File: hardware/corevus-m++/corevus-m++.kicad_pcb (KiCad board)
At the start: 4 copper layers, 100 x 64 mm, 154 parts, among them J1 XH, J2 XH, J3 USB 2.0, J4 Power In, J5 Power In, J6 1x2P, SW1 RST, SW2 BOOT, T1 V_{SA}, T10 MOSI, T11 Gnd, T12 MISO, T13 3.3V, T14 Therm, T15 V_{SA}, T16 SClk, T17 MOSI, T18 Gnd, T19 MISO, T2 SClk, T20 3.3V, T21 Therm, T22 V_{SA}, T23 SClk, T24 MOSI, T25 Gnd, T26 MISO, T27 3.3V, T28 Therm, T29 CS, T3 MOSI, T30 CS, T31 CS, T32 CS, T33 CS, T34 CS, T35 CS, T36 CS, T37 En, T38 En, T39 En, T4 Gnd, T40 En, T41 En, T42 En, T43 En, T44 En, T45 Dir, T46 Dir, T47 Dir, T48 Dir, T49 Dir, T5 MISO, T50 Dir, T51 Dir, T52 Dir, T53 Gnd, T54 Gnd, T55 Gnd, T56 Gnd, T57 Gnd, T58 Gnd, T59 Gnd, T6 3.3V, T60 Gnd, T61 Step, T62 Step, T63 Step, T64 Step, T65 Step, T66 Step, T67 Step, T68 Step, T69 Diag, T7 Therm, T70 Diag, T71 Diag, T72 Diag, T73 Diag, T74 Diag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

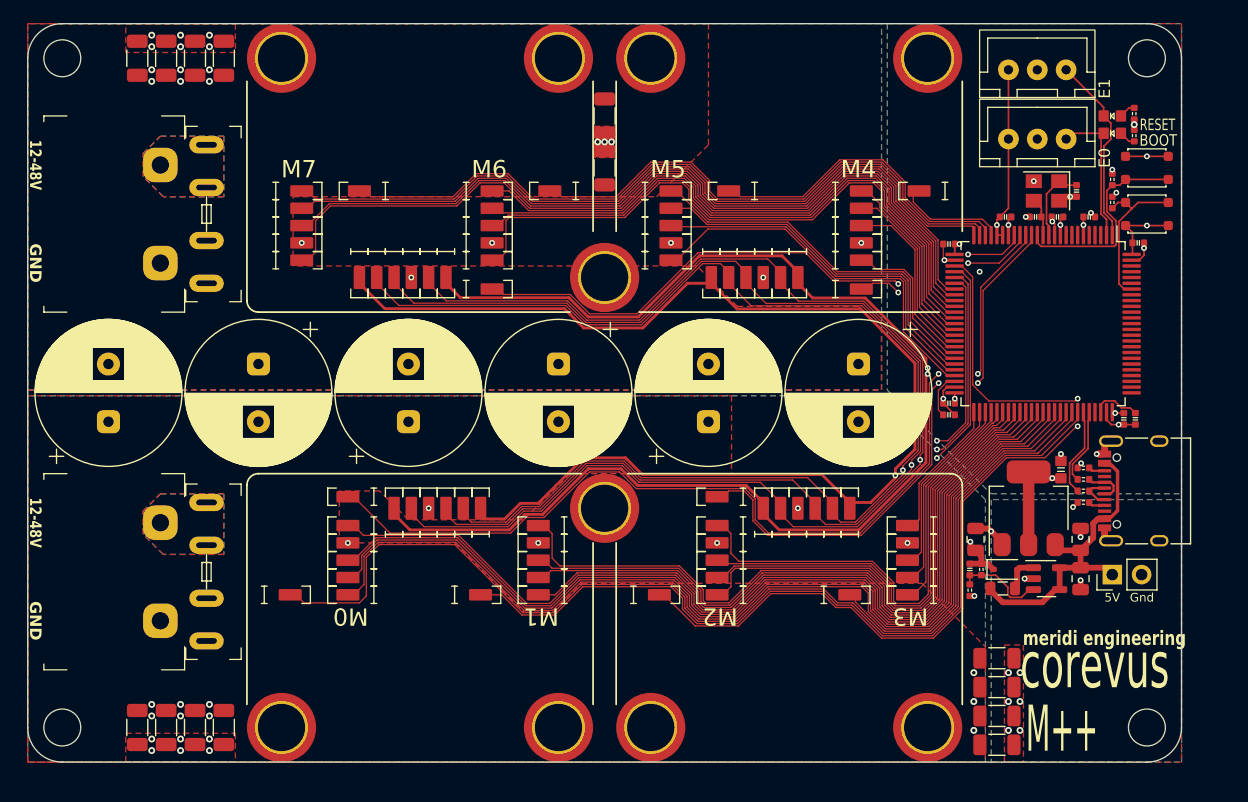
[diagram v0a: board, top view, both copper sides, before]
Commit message: corevus toolboard v0.2 release (working), corevus-g v0.2 release (very much not working), m++ v0.1 (not working, needs a lot of bodges)
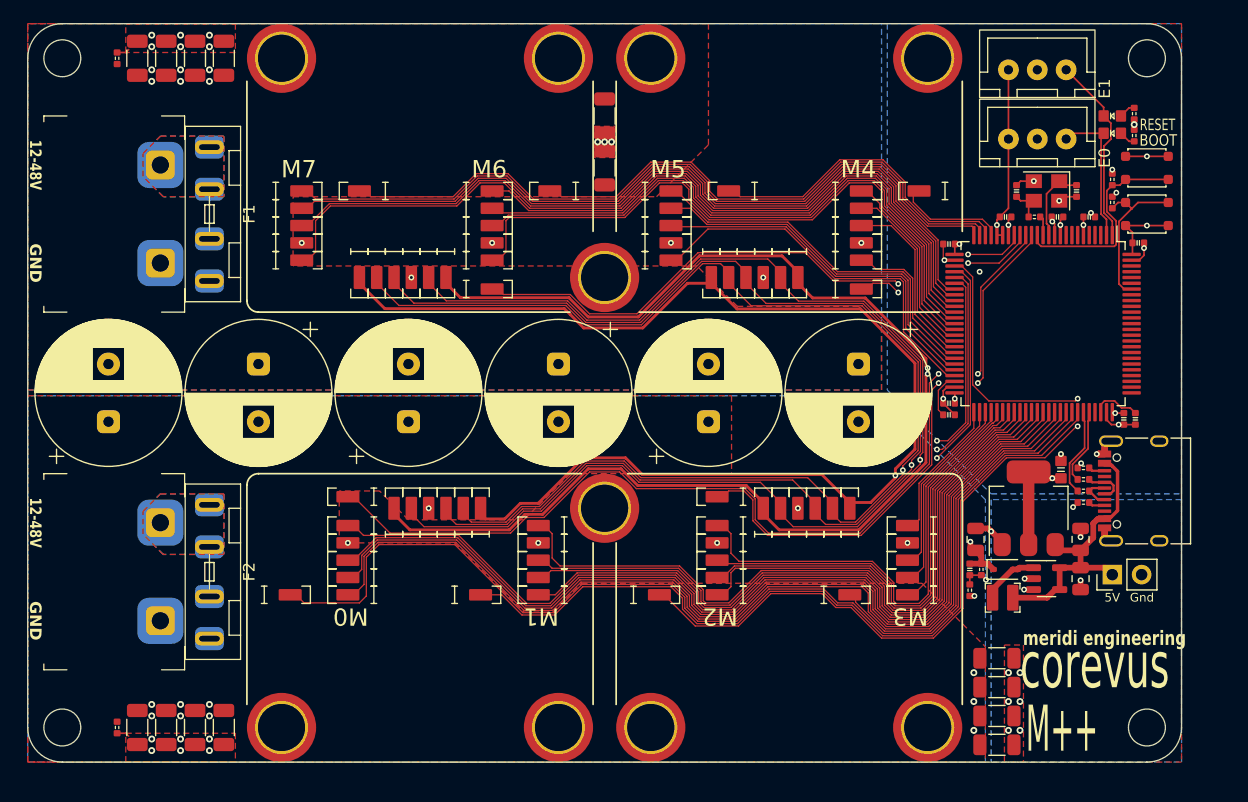
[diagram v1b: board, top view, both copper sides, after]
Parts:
- added R11: 1kΩ, AlphaLib:0402R, F.Cu at (197.2, 46.8)
- added R12: 200kΩ, AlphaLib:0402R, F.Cu at (117.8, 33.0)
- added R13: 200kΩ, AlphaLib:0402R, F.Cu at (117.8, 91.0)
- C11, C12, C13, C14, C15, C16: value 470μF 63V -> 390μF 63V
- C3, C4: value 15pF -> 16pF
- F1, F2: footprint corevus:XF-505P -> corevus:XF-506P
- L1: footprint Inductor_SMD:L_0805_2012Metric -> corevus:L_Changjiang_FTC2520
- T69, T70, T71, T72, T73, T74, T75, T76: value Diag -> Stall
- Y1: value 12 MHz -> 25 MHz
- moved C4 2.79 mm to (195.7, 44.5), turned to -90 degrees
- moved L1 0.80 mm to (194.5, 79.8)
- moved F1 0.25 mm to (125.8, 46.5)
- moved F2 0.25 mm to (125.8, 77.5)
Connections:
- net /_{M0}Diag renamed /_{M0}Stall
- net /_{M1}Diag renamed /_{M1}Stall
- net /_{M2}Diag renamed /_{M2}Stall
- net /_{M3}Diag renamed /_{M3}Stall
- net /_{M4}Diag renamed /_{M4}Stall
- net /_{M5}Diag renamed /_{M5}Stall
- net /_{M6}Diag renamed /_{M6}Stall
- net /_{M7}Diag renamed /_{M7}Stall
- C4 pad 2: Net-(U3-PH1) -> Net-(C4-Pad2)
- Y1 pad 3: Net-(U3-PH1) -> Net-(C4-Pad2)
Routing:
- net GND: track 31.8 -> 35.3 mm, vias 55 -> 54
- net Net-(C4-Pad2): track 0.00 -> 3.23 mm
- net +5V: track 27.4 -> 24.7 mm
- net Net-(D3-A): track 3.17 -> 5.03 mm
- net Net-(U3-PH1): track 3.34 -> 1.64 mm
- net Net-(U2-FB): track 7.40 -> 6.83 mm, vias 0 -> 2
